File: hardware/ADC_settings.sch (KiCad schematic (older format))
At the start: 10 parts

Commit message: Assigning footprints
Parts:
- R14, R15, R16, R17, R18, R19, R20, R21, R22, R23: renamed from R?; footprint (none) -> Resistor_SMD:R_0805_2012Metric
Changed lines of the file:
@@
 P 850 1400
 AR Path="/5E22D897/5E77AEF6" Ref="R?"  Part="1"
-AR Path="/5E22D897/5E776450/5E77AEF6" Ref="R?"  Part="1"
-F 0 "R?" H 920 1446 50  0000 L CNN
+AR Path="/5E22D897/5E776450/5E77AEF6" Ref="R14"  Part="1"
+F 0 "R14" H 920 1446 50  0000 L CNN
 F 1 "R0" H 920 1355 50  0000 L CNN
-F 2 "" V 780 1400 50  0001 C CNN
+F 2 "Resistor_SMD:R_0805_2012Metric" V 780 1400 50  0001 C CNN
 F 3 "~" H 850 1400 50  0001 C CNN
 	1    850  1400
@@
 P 850 1900
 AR Path="/5E22D897/5E77AEFD" Ref="R?"  Part="1"
-AR Path="/5E22D897/5E776450/5E77AEFD" Ref="R?"  Part="1"
-F 0 "R?" H 920 1946 50  0000 L CNN
+AR Path="/5E22D897/5E776450/5E77AEFD" Ref="R15"  Part="1"
+F 0 "R15" H 920 1946 50  0000 L CNN
 F 1 "R0" H 920 1855 50  0000 L CNN
-F 2 "" V 780 1900 50  0001 C CNN
+F 2 "Resistor_SMD:R_0805_2012Metric" V 780 1900 50  0001 C CNN
 F 3 "~" H 850 1900 50  0001 C CNN
 	1    850  1900
@@
 P 1650 1400
 AR Path="/5E22D897/5E77AF0D" Ref="R?"  Part="1"
-AR Path="/5E22D897/5E776450/5E77AF0D" Ref="R?"  Part="1"
-F 0 "R?" H 1720 1446 50  0000 L CNN
+AR Path="/5E22D897/5E776450/5E77AF0D" Ref="R16"  Part="1"
+F 0 "R16" H 1720 1446 50  0000 L CNN
 F 1 "R0" H 1720 1355 50  0000 L CNN
-F 2 "" V 1580 1400 50  0001 C CNN
+F 2 "Resistor_SMD:R_0805_2012Metric" V 1580 1400 50  0001 C CNN
 F 3 "~" H 1650 1400 50  0001 C CNN
 	1    1650 1400
@@
 P 1650 1900
 AR Path="/5E22D897/5E77AF14" Ref="R?"  Part="1"
-AR Path="/5E22D897/5E776450/5E77AF14" Ref="R?"  Part="1"
-F 0 "R?" H 1720 1946 50  0000 L CNN
+AR Path="/5E22D897/5E776450/5E77AF14" Ref="R17"  Part="1"
+F 0 "R17" H 1720 1946 50  0000 L CNN
 F 1 "R0" H 1720 1855 50  0000 L CNN
-F 2 "" V 1580 1900 50  0001 C CNN
+F 2 "Resistor_SMD:R_0805_2012Metric" V 1580 1900 50  0001 C CNN
 F 3 "~" H 1650 1900 50  0001 C CNN
 	1    1650 1900
@@
 P 4300 1400
 AR Path="/5E22D897/5E77AF25" Ref="R?"  Part="1"
-AR Path="/5E22D897/5E776450/5E77AF25" Ref="R?"  Part="1"
-F 0 "R?" H 4370 1446 50  0000 L CNN
+AR Path="/5E22D897/5E776450/5E77AF25" Ref="R22"  Part="1"
+F 0 "R22" H 4370 1446 50  0000 L CNN
 F 1 "R0" H 4370 1355 50  0000 L CNN
-F 2 "" V 4230 1400 50  0001 C CNN
+F 2 "Resistor_SMD:R_0805_2012Metric" V 4230 1400 50  0001 C CNN
 F 3 "~" H 4300 1400 50  0001 C CNN
 	1    4300 1400
@@
 P 4300 1900
 AR Path="/5E22D897/5E77AF2C" Ref="R?"  Part="1"
-AR Path="/5E22D897/5E776450/5E77AF2C" Ref="R?"  Part="1"
-F 0 "R?" H 4370 1946 50  0000 L CNN
+AR Path="/5E22D897/5E776450/5E77AF2C" Ref="R23"  Part="1"
+F 0 "R23" H 4370 1946 50  0000 L CNN
 F 1 "R0" H 4370 1855 50  0000 L CNN
-F 2 "" V 4230 1900 50  0001 C CNN
+F 2 "Resistor_SMD:R_0805_2012Metric" V 4230 1900 50  0001 C CNN
 F 3 "~" H 4300 1900 50  0001 C CNN
 	1    4300 1900
@@
 P 3300 1400
 AR Path="/5E22D897/5E77AF3C" Ref="R?"  Part="1"
-AR Path="/5E22D897/5E776450/5E77AF3C" Ref="R?"  Part="1"
-F 0 "R?" H 3370 1446 50  0000 L CNN
+AR Path="/5E22D897/5E776450/5E77AF3C" Ref="R20"  Part="1"
+F 0 "R20" H 3370 1446 50  0000 L CNN
 F 1 "R0" H 3370 1355 50  0000 L CNN
-F 2 "" V 3230 1400 50  0001 C CNN
+F 2 "Resistor_SMD:R_0805_2012Metric" V 3230 1400 50  0001 C CNN
 F 3 "~" H 3300 1400 50  0001 C CNN
 	1    3300 1400
@@
 P 3300 1900
 AR Path="/5E22D897/5E77AF43" Ref="R?"  Part="1"
-AR Path="/5E22D897/5E776450/5E77AF43" Ref="R?"  Part="1"
-F 0 "R?" H 3370 1946 50  0000 L CNN
+AR Path="/5E22D897/5E776450/5E77AF43" Ref="R21"  Part="1"
+F 0 "R21" H 3370 1946 50  0000 L CNN
 F 1 "R0" H 3370 1855 50  0000 L CNN
-F 2 "" V 3230 1900 50  0001 C CNN
+F 2 "Resistor_SMD:R_0805_2012Metric" V 3230 1900 50  0001 C CNN
 F 3 "~" H 3300 1900 50  0001 C CNN
 	1    3300 1900
@@
 P 2400 1400
 AR Path="/5E22D897/5E77AF53" Ref="R?"  Part="1"
-AR Path="/5E22D897/5E776450/5E77AF53" Ref="R?"  Part="1"
-F 0 "R?" H 2470 1446 50  0000 L CNN
+AR Path="/5E22D897/5E776450/5E77AF53" Ref="R18"  Part="1"
+F 0 "R18" H 2470 1446 50  0000 L CNN
 F 1 "R0" H 2470 1355 50  0000 L CNN
-F 2 "" V 2330 1400 50  0001 C CNN
+F 2 "Resistor_SMD:R_0805_2012Metric" V 2330 1400 50  0001 C CNN
 F 3 "~" H 2400 1400 50  0001 C CNN
 	1    2400 1400
@@
 P 2400 1900
 AR Path="/5E22D897/5E77AF5A" Ref="R?"  Part="1"
-AR Path="/5E22D897/5E776450/5E77AF5A" Ref="R?"  Part="1"
-F 0 "R?" H 2470 1946 50  0000 L CNN
+AR Path="/5E22D897/5E776450/5E77AF5A" Ref="R19"  Part="1"
+F 0 "R19" H 2470 1946 50  0000 L CNN
 F 1 "R0" H 2470 1855 50  0000 L CNN
-F 2 "" V 2330 1900 50  0001 C CNN
+F 2 "Resistor_SMD:R_0805_2012Metric" V 2330 1900 50  0001 C CNN
 F 3 "~" H 2400 1900 50  0001 C CNN
 	1    2400 1900

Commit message: Adding last known changes to shematics
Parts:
- removed R14, R15, R16, R17, R18, R19, R20, R21, R22, R23: R0, Resistor_SMD:R_0805_2012Metric, symbol antena:R
- added J?: PAR, symbol Connector_Generic:Conn_01x03
- added J?: RANGE, symbol Connector_Generic:Conn_01x03
- added J?: REF, symbol Connector_Generic:Conn_01x03
- added J?: OS0, symbol Connector_Generic:Conn_01x03
- added J?: OS1, symbol Connector_Generic:Conn_01x03
- added J?: OS2, symbol Connector_Generic:Conn_01x03
- added R? (x7): 1K, Resistor_SMD:R_0805_2012Metric, symbol antena:R
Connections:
- net ADC_PAR: now also R?.1
- net ADC_RANGE: now also R?.1
- net ADC_REF_EN_WR: now also R?.1
- net ADC_STBY: now also R?.1
- net AGND: now also J?.1 (Pin_1), J?.1 (Pin_1), J?.1 (Pin_1), J?.1 (Pin_1), J?.1 (Pin_1), J?.1 (Pin_1)
- new net: J?.2 (Pin_2), R?.2 (x6)
- new net AVDD: J?.3 (Pin_3), J?.3 (Pin_3), J?.3 (Pin_3), J?.3 (Pin_3), J?.3 (Pin_3), J?.3 (Pin_3), R?.2
- new net OS0: R?.1
- new net OS1: R?.1
- new net OS2: R?.1
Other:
- note added: "+-5(0)/+-10(1)"
- note added: "Oversampling"
- note removed: "+-4(0)/+-2(1) VREF"
- note removed: "HW(0)/SW(1)"
- note removed: "WORD(0)/BYTE(1)"

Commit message: Routing board
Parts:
- J10, J11, J12, J13, J14, J15: renamed from J?; footprint (none) -> Connector_PinHeader_2.00mm:PinHeader_1x03_P2.00mm_Vertical
- gave numbers to parts that had none: 7
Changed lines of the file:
@@
 P 3100 1600
 AR Path="/5E22D897/5E5B7CE6" Ref="R?"  Part="1"
-AR Path="/5E22D897/5E776450/5E5B7CE6" Ref="R?"  Part="1"
-F 0 "R?" V 3200 1550 50  0000 L CNN
+AR Path="/5E22D897/5E776450/5E5B7CE6" Ref="R20"  Part="1"
+F 0 "R20" V 3200 1550 50  0000 L CNN
 F 1 "1K" V 3000 1550 50  0000 L CNN
 F 2 "Resistor_SMD:R_0805_2012Metric" V 3030 1600 50  0001 C CNN
@@
 P 5450 1650
 AR Path="/5E22D897/5E5B7D54" Ref="R?"  Part="1"
-AR Path="/5E22D897/5E776450/5E5B7D54" Ref="R?"  Part="1"
-F 0 "R?" H 5520 1696 50  0000 L CNN
+AR Path="/5E22D897/5E776450/5E5B7D54" Ref="R23"  Part="1"
+F 0 "R23" H 5520 1696 50  0000 L CNN
 F 1 "1K" H 5520 1605 50  0000 L CNN
 F 2 "Resistor_SMD:R_0805_2012Metric" V 5380 1650 50  0001 C CNN
@@
 	5350 2350 5650 2350
 $Comp
-L Connector_Generic:Conn_01x03 J?
+L Connector_Generic:Conn_01x03 J13
 U 1 1 5E67A1EB
 P 3100 2000
-F 0 "J?" H 3020 1675 50  0000 C CNN
+F 0 "J13" H 3020 1675 50  0000 C CNN
 F 1 "PAR" H 3020 1766 50  0000 C CNN
-F 2 "" H 3100 2000 50  0001 C CNN
+F 2 "Connector_PinHeader_2.00mm:PinHeader_1x03_P2.00mm_Vertical" H 3100 2000 50  0001 C CNN
 F 3 "~" H 3100 2000 50  0001 C CNN
 	1    3100 2000
@@
 P 3850 1600
 AR Path="/5E22D897/5E67C00C" Ref="R?"  Part="1"
-AR Path="/5E22D897/5E776450/5E67C00C" Ref="R?"  Part="1"
-F 0 "R?" V 3950 1550 50  0000 L CNN
+AR Path="/5E22D897/5E776450/5E67C00C" Ref="R21"  Part="1"
+F 0 "R21" V 3950 1550 50  0000 L CNN
 F 1 "1K" V 3750 1550 50  0000 L CNN
 F 2 "Resistor_SMD:R_0805_2012Metric" V 3780 1600 50  0001 C CNN
@@
 $EndComp
 $Comp
-L Connector_Generic:Conn_01x03 J?
+L Connector_Generic:Conn_01x03 J14
 U 1 1 5E67C012
 P 3850 2000
-F 0 "J?" V 3723 2180 50  0000 L CNN
+F 0 "J14" V 3723 2180 50  0000 L CNN
 F 1 "RANGE" V 3814 2180 50  0000 L CNN
-F 2 "" H 3850 2000 50  0001 C CNN
+F 2 "Connector_PinHeader_2.00mm:PinHeader_1x03_P2.00mm_Vertical" H 3850 2000 50  0001 C CNN
 F 3 "~" H 3850 2000 50  0001 C CNN
 	1    3850 2000
@@
 P 4800 1700
 AR Path="/5E22D897/5E67DDE2" Ref="R?"  Part="1"
-AR Path="/5E22D897/5E776450/5E67DDE2" Ref="R?"  Part="1"
-F 0 "R?" V 4900 1650 50  0000 L CNN
+AR Path="/5E22D897/5E776450/5E67DDE2" Ref="R22"  Part="1"
+F 0 "R22" V 4900 1650 50  0000 L CNN
 F 1 "1K" V 4700 1650 50  0000 L CNN
 F 2 "Resistor_SMD:R_0805_2012Metric" V 4730 1700 50  0001 C CNN
@@
 $EndComp
 $Comp
-L Connector_Generic:Conn_01x03 J?
+L Connector_Generic:Conn_01x03 J15
 U 1 1 5E67DDE8
 P 4800 2100
-F 0 "J?" V 4673 2280 50  0000 L CNN
+F 0 "J15" V 4673 2280 50  0000 L CNN
 F 1 "REF" V 4764 2280 50  0000 L CNN
-F 2 "" H 4800 2100 50  0001 C CNN
+F 2 "Connector_PinHeader_2.00mm:PinHeader_1x03_P2.00mm_Vertical" H 4800 2100 50  0001 C CNN
 F 3 "~" H 4800 2100 50  0001 C CNN
 	1    4800 2100
@@
 P 1050 1600
 AR Path="/5E22D897/5E6865E6" Ref="R?"  Part="1"
-AR Path="/5E22D897/5E776450/5E6865E6" Ref="R?"  Part="1"
-F 0 "R?" V 1150 1550 50  0000 L CNN
+AR Path="/5E22D897/5E776450/5E6865E6" Ref="R17"  Part="1"
+F 0 "R17" V 1150 1550 50  0000 L CNN
 F 1 "1K" V 950 1550 50  0000 L CNN
 F 2 "Resistor_SMD:R_0805_2012Metric" V 980 1600 50  0001 C CNN
@@
 $EndComp
 $Comp
-L Connector_Generic:Conn_01x03 J?
+L Connector_Generic:Conn_01x03 J10
 U 1 1 5E6865EC
 P 1050 2000
-F 0 "J?" V 923 2180 50  0000 L CNN
+F 0 "J10" V 923 2180 50  0000 L CNN
 F 1 "OS0" V 1014 2180 50  0000 L CNN
-F 2 "" H 1050 2000 50  0001 C CNN
+F 2 "Connector_PinHeader_2.00mm:PinHeader_1x03_P2.00mm_Vertical" H 1050 2000 50  0001 C CNN
 F 3 "~" H 1050 2000 50  0001 C CNN
 	1    1050 2000
@@
 P 1650 1600
 AR Path="/5E22D897/5E686A55" Ref="R?"  Part="1"
-AR Path="/5E22D897/5E776450/5E686A55" Ref="R?"  Part="1"
-F 0 "R?" V 1750 1550 50  0000 L CNN
+AR Path="/5E22D897/5E776450/5E686A55" Ref="R18"  Part="1"
+F 0 "R18" V 1750 1550 50  0000 L CNN
 F 1 "1K" V 1550 1550 50  0000 L CNN
 F 2 "Resistor_SMD:R_0805_2012Metric" V 1580 1600 50  0001 C CNN
@@
 $EndComp
 $Comp
-L Connector_Generic:Conn_01x03 J?
+L Connector_Generic:Conn_01x03 J11
 U 1 1 5E686A5B
 P 1650 2000
-F 0 "J?" V 1523 2180 50  0000 L CNN
+F 0 "J11" V 1523 2180 50  0000 L CNN
 F 1 "OS1" V 1614 2180 50  0000 L CNN
-F 2 "" H 1650 2000 50  0001 C CNN
+F 2 "Connector_PinHeader_2.00mm:PinHeader_1x03_P2.00mm_Vertical" H 1650 2000 50  0001 C CNN
 F 3 "~" H 1650 2000 50  0001 C CNN
 	1    1650 2000
@@
 P 2200 1600
 AR Path="/5E22D897/5E687074" Ref="R?"  Part="1"
-AR Path="/5E22D897/5E776450/5E687074" Ref="R?"  Part="1"
-F 0 "R?" V 2300 1550 50  0000 L CNN
+AR Path="/5E22D897/5E776450/5E687074" Ref="R19"  Part="1"
+F 0 "R19" V 2300 1550 50  0000 L CNN
 F 1 "1K" V 2100 1550 50  0000 L CNN
 F 2 "Resistor_SMD:R_0805_2012Metric" V 2130 1600 50  0001 C CNN
@@
 $EndComp
 $Comp
-L Connector_Generic:Conn_01x03 J?
+L Connector_Generic:Conn_01x03 J12
 U 1 1 5E68707A
 P 2200 2000
-F 0 "J?" V 2073 2180 50  0000 L CNN
+F 0 "J12" V 2073 2180 50  0000 L CNN
 F 1 "OS2" V 2164 2180 50  0000 L CNN
-F 2 "" H 2200 2000 50  0001 C CNN
+F 2 "Connector_PinHeader_2.00mm:PinHeader_1x03_P2.00mm_Vertical" H 2200 2000 50  0001 C CNN
 F 3 "~" H 2200 2000 50  0001 C CNN
 	1    2200 2000

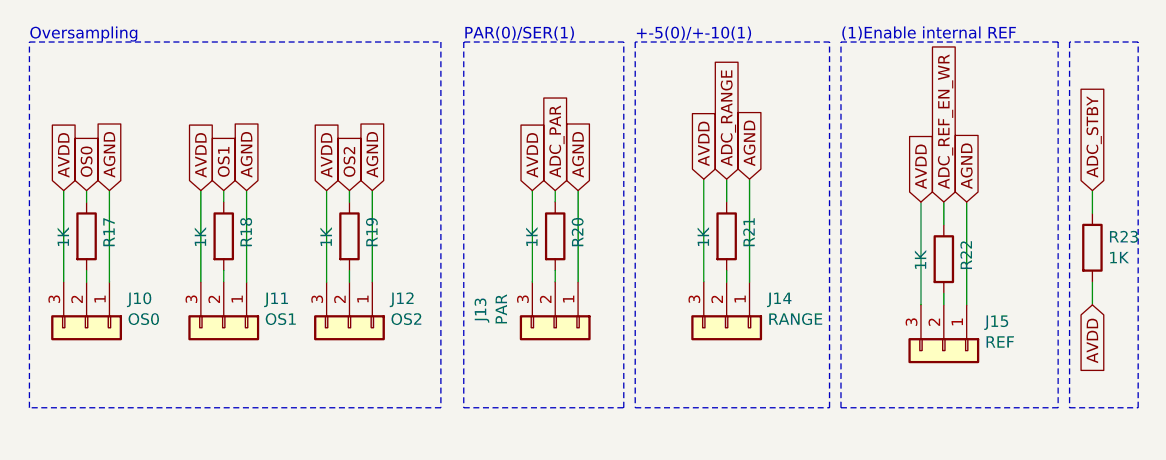
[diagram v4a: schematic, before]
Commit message: Finishing routing
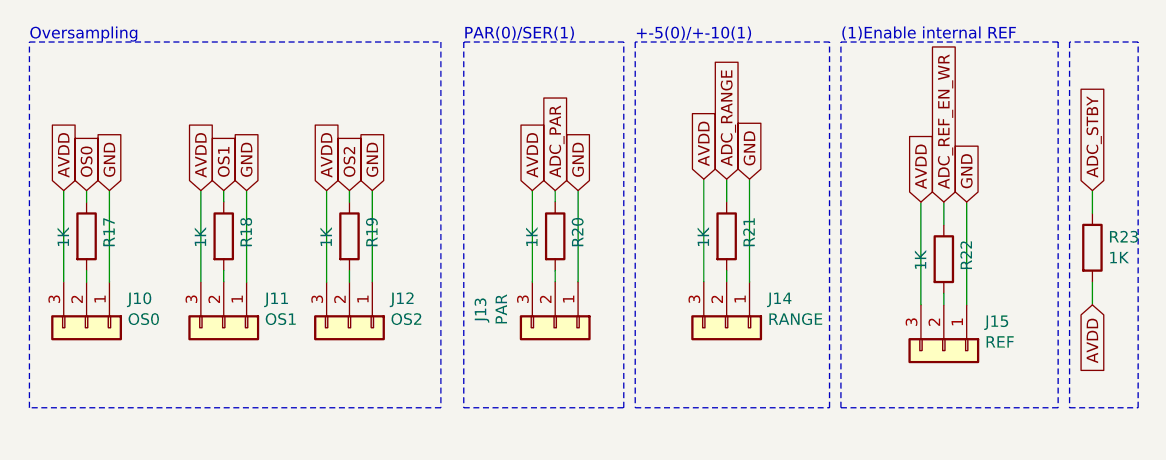
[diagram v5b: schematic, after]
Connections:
- net AGND renamed GND
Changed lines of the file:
@@
 $EndDescr
 Text GLabel 3200 1400 1    50   Input ~ 0
-AGND
+GND
 Text GLabel 3000 1400 1    50   Input ~ 0
 AVDD
@@
 ADC_REF_EN_WR
 Text GLabel 4900 1450 1    50   Input ~ 0
-AGND
+GND
 Text GLabel 4700 1450 1    50   Input ~ 0
 AVDD
@@
 ADC_RANGE
 Text GLabel 3950 1350 1    50   Input ~ 0
-AGND
+GND
 Text GLabel 3750 1350 1    50   Input ~ 0
 AVDD
@@
 AVDD
 Text GLabel 1150 1400 1    50   Input ~ 0
-AGND
+GND
 Text GLabel 1550 1400 1    50   Input ~ 0
 AVDD
 Text GLabel 1750 1400 1    50   Input ~ 0
-AGND
+GND
 Text GLabel 2100 1400 1    50   Input ~ 0
 AVDD
 Text GLabel 2300 1400 1    50   Input ~ 0
-AGND
+GND
 Wire Notes Line
 	2600 750  2600 2350
